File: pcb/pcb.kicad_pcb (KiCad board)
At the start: 2 copper layers, 48.5 x 50.4 mm, 17 parts, among them J1 OLED, J2 Thermocouple, J3 Interupt, J4 UART, Q1 NPN, Q2 NPN, U2 MAX6675ISA_, U5 WEMOS_D1_mini

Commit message: updated changes in pcb
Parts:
- removed Q2: NPN, Package_TO_SOT_SMD:SOT-23-3
- R5: footprint Resistor_THT:R_Axial_DIN0207_L6.3mm_D2.5mm_P10.16mm_Horizontal -> Resistor_SMD:R_1206_3216Metric_Pad1.30x1.75mm_HandSolder; moved to B.Cu
- moved Q1 9.43 mm to (138.2, 111.1), turned to -90 degrees
- moved R5 0.11 mm to (135.0, 113.9), turned to 90 degrees
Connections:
- BZ1 pad 2: Net-(Q2-C) -> Net-(Q1-C)
- R5 pad 1: Net-(Q1-C) -> GND
- R5 pad 2: +5V -> Net-(Q1-B)
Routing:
- net Net-(Q1-B): track 2.99 -> 16.3 mm
- net Net-(Q2-C): track 10.4 -> 0.00 mm
- net Net-(Q1-C): track 13.2 -> 6.42 mm

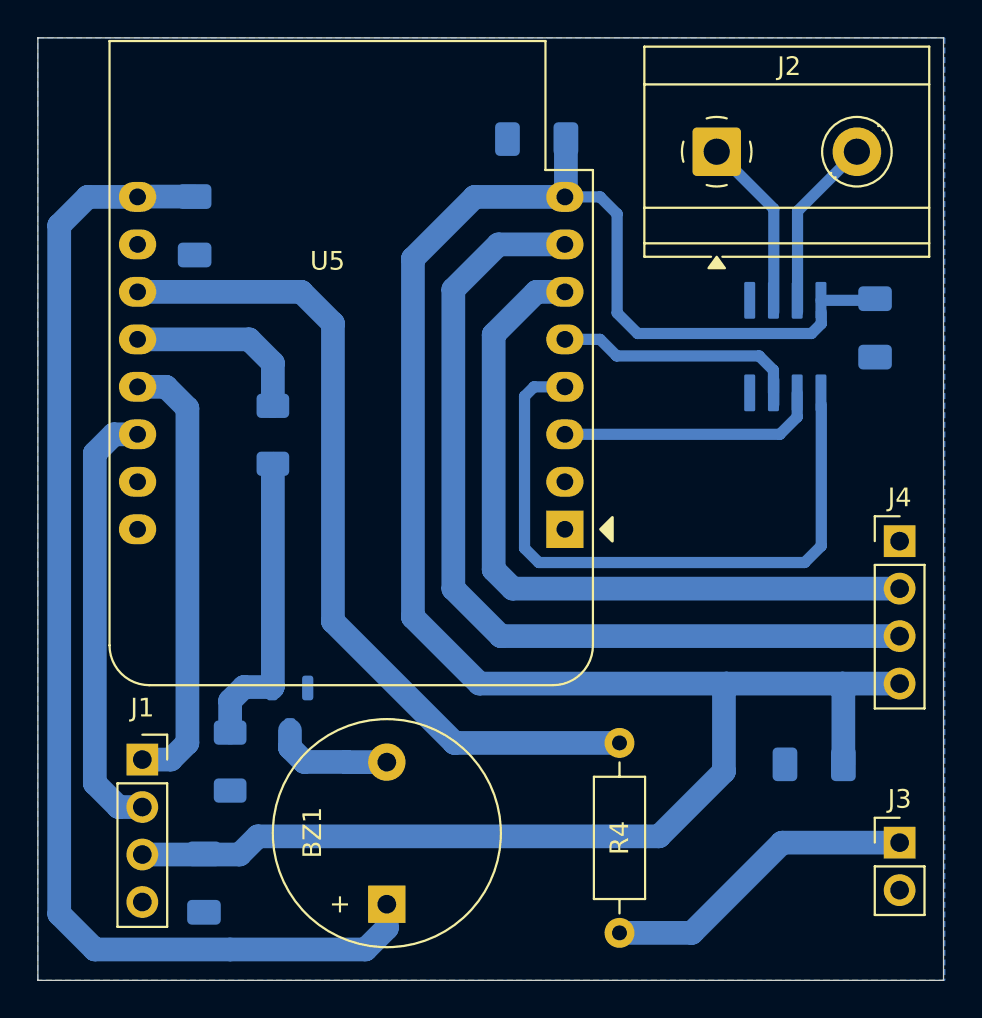
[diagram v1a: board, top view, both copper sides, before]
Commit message: added battery functionality, updated pcb
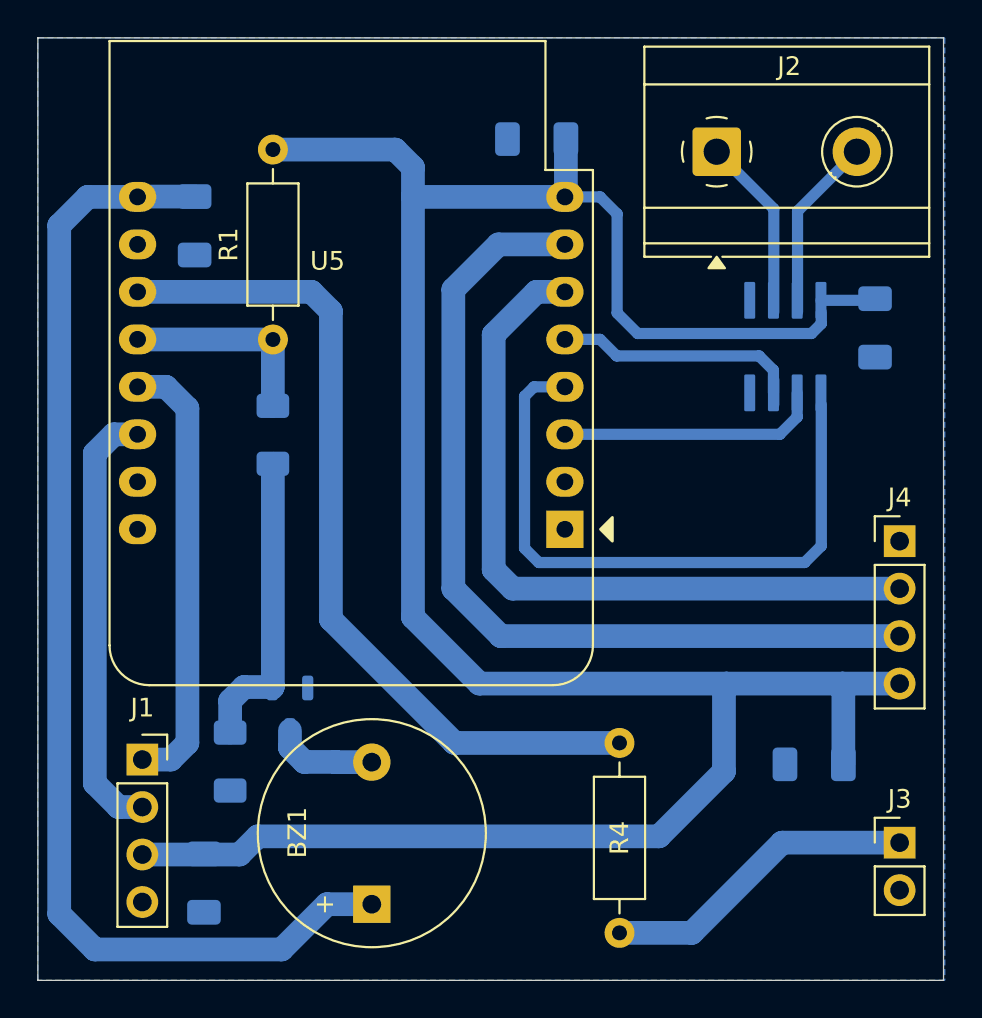
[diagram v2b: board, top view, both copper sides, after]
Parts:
- removed R5: 10k, Resistor_SMD:R_1206_3216Metric_Pad1.30x1.75mm_HandSolder
- added R1: 10k, Resistor_THT:R_Axial_DIN0207_L6.3mm_D2.5mm_P10.16mm_Horizontal, F.Cu at (137.3, 91.3)
- added R2: 10k, Resistor_SMD:R_1206_3216Metric_Pad1.30x1.75mm_HandSolder, B.Cu at (135.0, 113.9)
- moved BZ1 0.80 mm to (142.6, 121.5)
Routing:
- net +3.3V: track 124.9 -> 136.3 mm
- net +5V: track 64.8 -> 63.2 mm
- net Net-(Q1-C): track 6.42 -> 5.62 mm
- net /GPIO0: track 10.1 -> 10.8 mm
